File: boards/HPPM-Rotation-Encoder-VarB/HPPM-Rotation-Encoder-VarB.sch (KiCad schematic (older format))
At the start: 13 parts, among them J1 CONN, U1 AS5045B, U2 DS9638

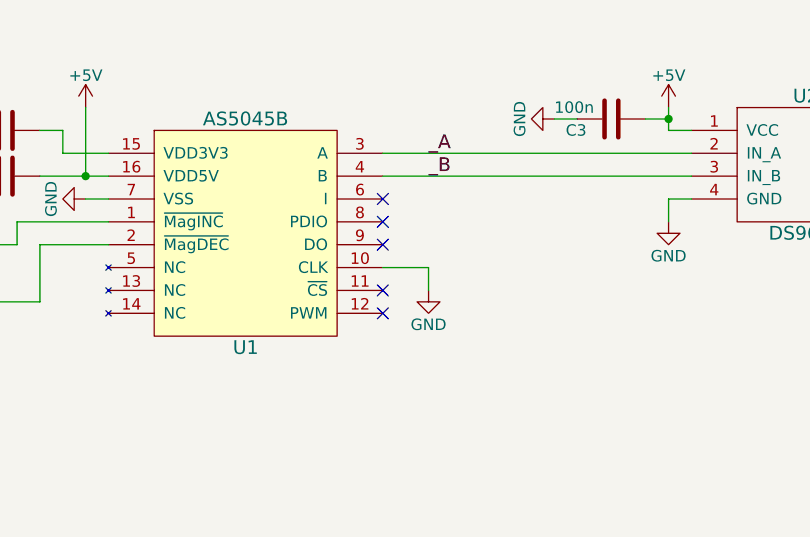
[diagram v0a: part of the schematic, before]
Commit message: [board][HPPM-Rotation-Encoder-Var*] minor fiixes: DRC and PDIO wired to GND
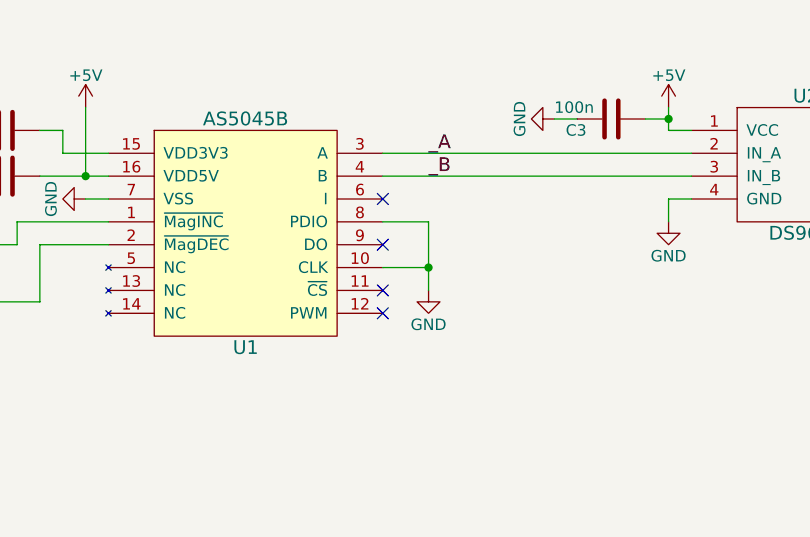
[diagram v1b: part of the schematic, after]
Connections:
- net GND: now also U1.8 (PDIO)
- no-connect marks 5 -> 4
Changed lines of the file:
@@
 NoConn ~ 6200 3550
 NoConn ~ 6200 3750
-NoConn ~ 6200 3650
 $Comp
 L GND #PWR015
@@
 $EndComp
 Wire Wire Line
-	6400 3950 6400 3850
+	6400 3650 6400 3950
 Wire Wire Line
 	6400 3850 6200 3850
@@
 	4900 3150 4900 3450
 Connection ~ 4900 3450
+Wire Wire Line
+	6200 3650 6400 3650
+Connection ~ 6400 3850
 $EndSCHEMATC
